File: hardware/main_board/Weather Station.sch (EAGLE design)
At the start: 38 parts, among them J2 RJ12, Q1 200mA/40V, Q2 220mA/50V/3.5Ω, U1 328P, U2 MCP1703T-3302E/CB, U3 W25X40CLSNIG, U4 TL431BQPK, X2 B2B-PH-K-S, X3 B2B-XH-2, Y1 8MHz

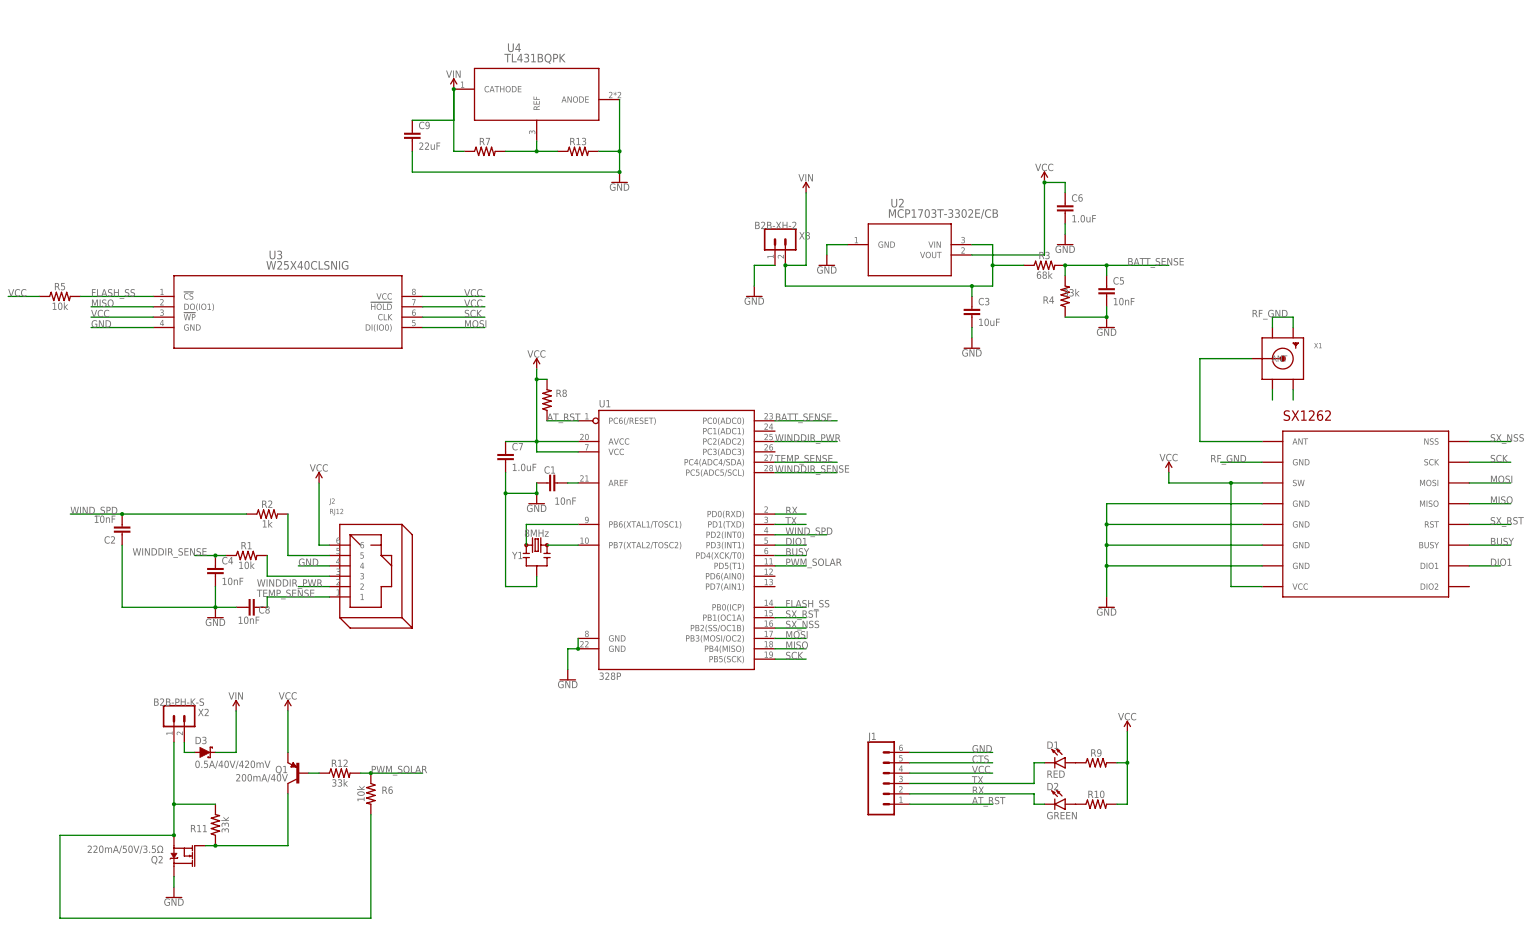
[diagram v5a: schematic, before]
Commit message: Better speed formatting for null values; Some other stuff
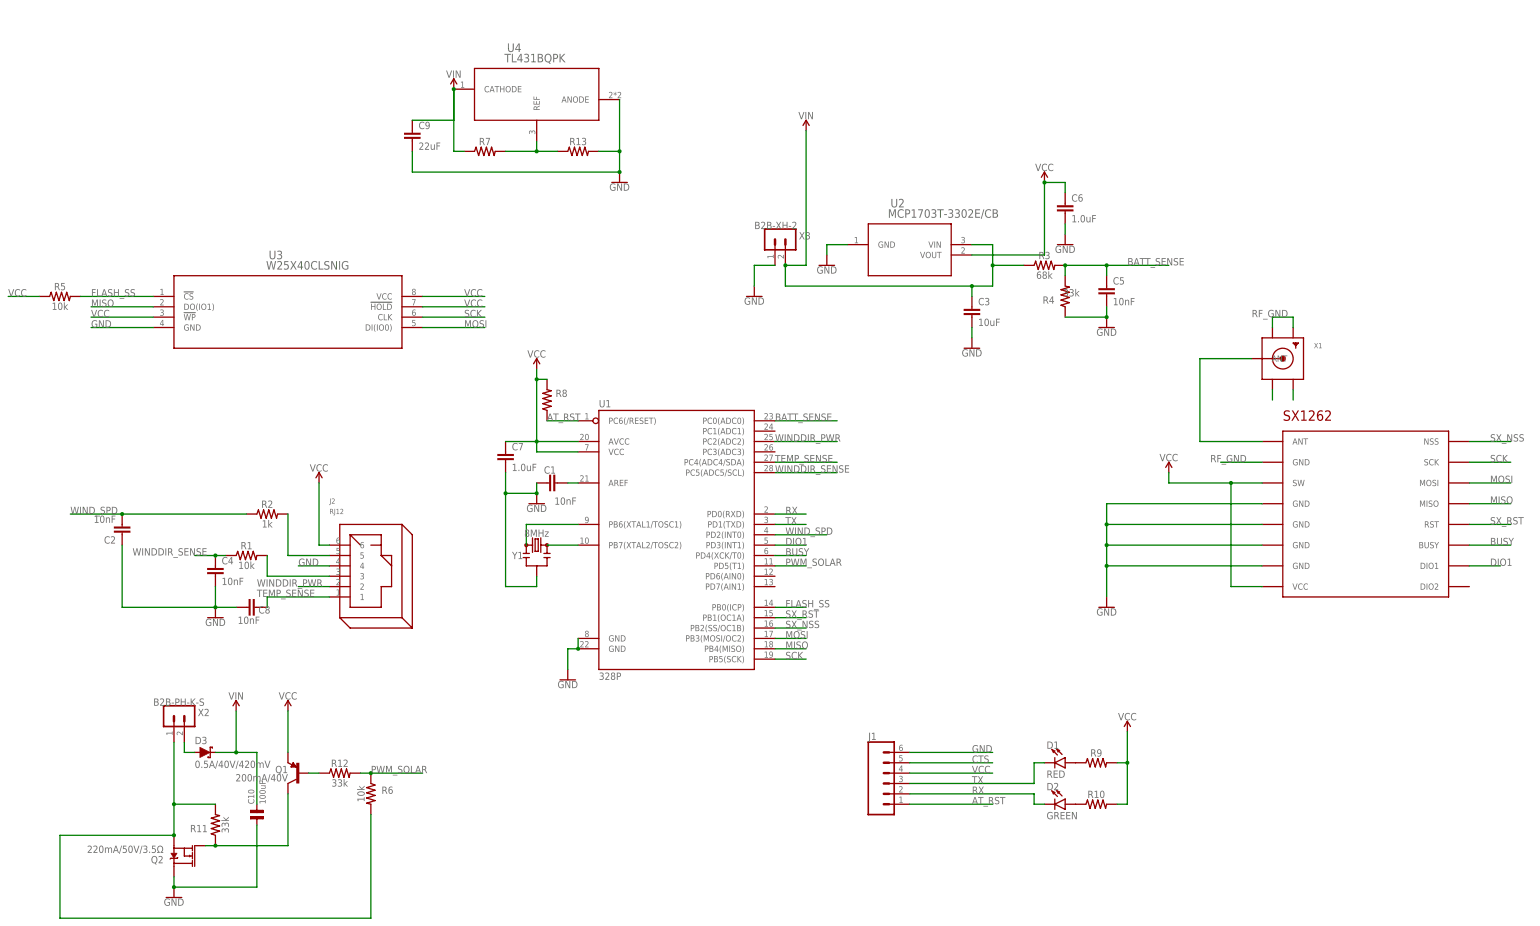
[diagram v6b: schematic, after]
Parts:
- added C10: 100uF, capsmd:C1206
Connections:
- net GND: now also C10.1
- net VIN: now also C10.2
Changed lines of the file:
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@@
 <part name="SUPPLY9" library="SparkFun-PowerSymbols" library_urn="urn:adsk.eagle:library:530" deviceset="VCC" device=""/>
 <part name="U$1" library="RadioShield" deviceset="SX1262" device=""/>
+<part name="C10" library="capsmd" deviceset="C1206" device="" value="100uF"/>
 </parts>
 <sheets>
@@
 <attribute name="VALUE" x="-45.72" y="-21.844" size="1.778" layer="96" font="vector" align="top-center"/>
 </instance>
-<instance part="SUPPLY5" gate="G$1" x="68.58" y="121.92" smashed="yes">
-<attribute name="VALUE" x="68.58" y="124.714" size="1.778" layer="96" align="bottom-center"/>
+<instance part="SUPPLY5" gate="G$1" x="68.58" y="137.16" smashed="yes">
+<attribute name="VALUE" x="68.58" y="139.954" size="1.778" layer="96" align="bottom-center"/>
 </instance>
 <instance part="SUPPLY7" gate="G$1" x="-71.12" y="-5.08" smashed="yes">
@@
 </instance>
 <instance part="U$1" gate="G$1" x="205.74" y="43.18" smashed="yes"/>
+<instance part="C10" gate="G$1" x="-66.04" y="-30.48" smashed="yes" rot="R90">
+<attribute name="NAME" x="-66.675" y="-27.94" size="1.524" layer="95" rot="R90"/>
+<attribute name="VALUE" x="-63.881" y="-27.94" size="1.524" layer="96" rot="R90"/>
+</instance>
 </instances>
 <busses>
@@
 </segment>
 <segment>
+<pinref part="GND8" gate="1" pin="GND"/>
 <pinref part="C3" gate="G$1" pin="2"/>
-<pinref part="GND8" gate="1" pin="GND"/>
 <wire x1="109.22" y1="88.9" x2="109.22" y2="86.36" width="0.1524" layer="91"/>
+</segment>
+<segment>
+<pinref part="C10" gate="G$1" pin="1"/>
+<pinref part="Q2" gate="NMOS" pin="D"/>
+<pinref part="GND10" gate="1" pin="GND"/>
+<wire x1="-86.36" y1="-45.72" x2="-86.36" y2="-48.26" width="0.1524" layer="91"/>
+<wire x1="-66.04" y1="-33.02" x2="-66.04" y2="-48.26" width="0.1524" layer="91"/>
+<wire x1="-66.04" y1="-48.26" x2="-86.36" y2="-48.26" width="0.1524" layer="91"/>
+<junction x="-86.36" y="-48.26"/>
 </segment>
 <segment>
@@
 <wire x1="-91.44" y1="88.9" x2="-106.68" y2="88.9" width="0.1524" layer="91"/>
 <label x="-106.68" y="88.9" size="1.778" layer="95"/>
-</segment>
-<segment>
-<pinref part="Q2" gate="NMOS" pin="D"/>
-<pinref part="GND10" gate="1" pin="GND"/>
-<wire x1="-86.36" y1="-45.72" x2="-86.36" y2="-48.26" width="0.1524" layer="91"/>
 </segment>
 <segment>
@@
 <net name="VIN" class="0">
 <segment>
+<pinref part="SUPPLY7" gate="G$1" pin="VIN"/>
+<pinref part="C10" gate="G$1" pin="2"/>
+<wire x1="-66.04" y1="-15.24" x2="-66.04" y2="-27.94" width="0.1524" layer="91"/>
+<pinref part="D3" gate="G$1" pin="C"/>
+<wire x1="-76.2" y1="-15.24" x2="-71.12" y2="-15.24" width="0.1524" layer="91"/>
+<wire x1="-71.12" y1="-15.24" x2="-66.04" y2="-15.24" width="0.1524" layer="91"/>
+<junction x="-71.12" y="-15.24"/>
+<wire x1="-71.12" y1="-15.24" x2="-71.12" y2="-5.08" width="0.1524" layer="91"/>
+</segment>
+<segment>
 <wire x1="63.5" y1="104.14" x2="63.5" y2="99.06" width="0.1524" layer="91"/>
 <wire x1="63.5" y1="99.06" x2="109.22" y2="99.06" width="0.1524" layer="91"/>
@@
 <wire x1="114.3" y1="109.22" x2="114.3" y2="104.14" width="0.1524" layer="91"/>
 <wire x1="63.5" y1="104.14" x2="68.58" y2="104.14" width="0.1524" layer="91"/>
-<wire x1="68.58" y1="104.14" x2="68.58" y2="121.92" width="0.1524" layer="91"/>
+<wire x1="68.58" y1="104.14" x2="68.58" y2="137.16" width="0.1524" layer="91"/>
 <junction x="63.5" y="104.14"/>
 <pinref part="SUPPLY5" gate="G$1" pin="VIN"/>
 </segment>
 <segment>
-<pinref part="D3" gate="G$1" pin="C"/>
-<pinref part="SUPPLY7" gate="G$1" pin="VIN"/>
-<wire x1="-76.2" y1="-15.24" x2="-71.12" y2="-15.24" width="0.1524" layer="91"/>
-<wire x1="-71.12" y1="-15.24" x2="-71.12" y2="-5.08" width="0.1524" layer="91"/>
-</segment>
-<segment>

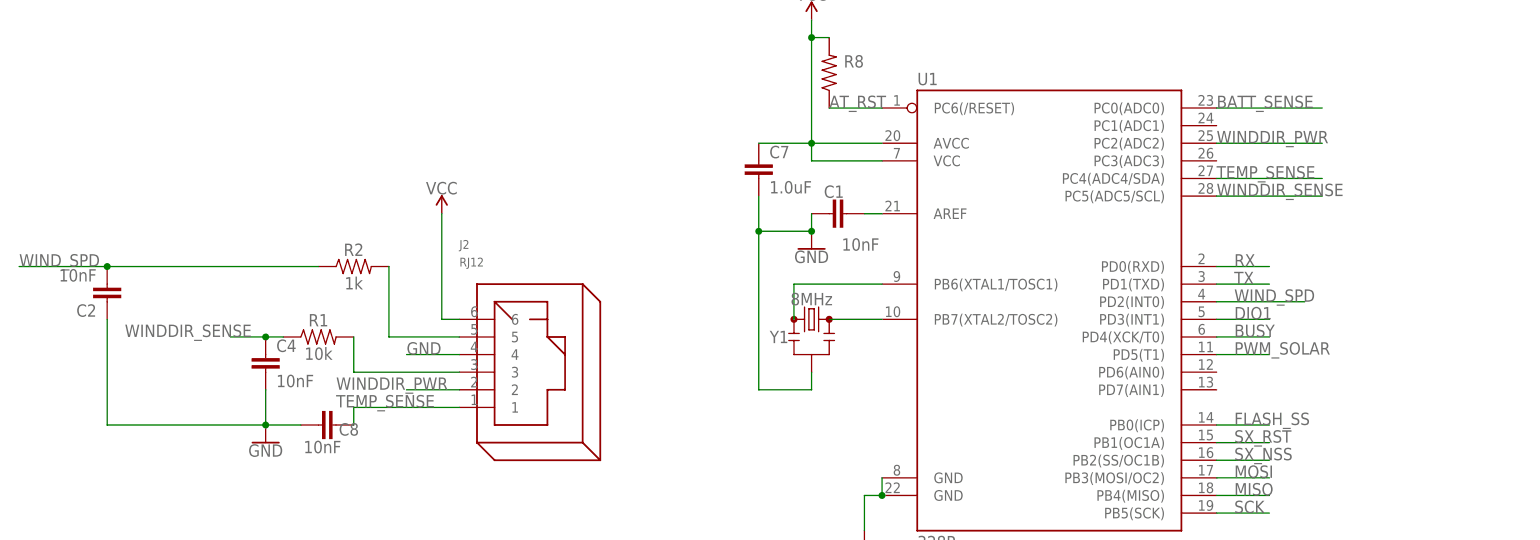
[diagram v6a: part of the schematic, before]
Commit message: ALS Wind direction bug fixes. Added ability to chain receivers using UDP. QueryVolatileResponse bugfix.
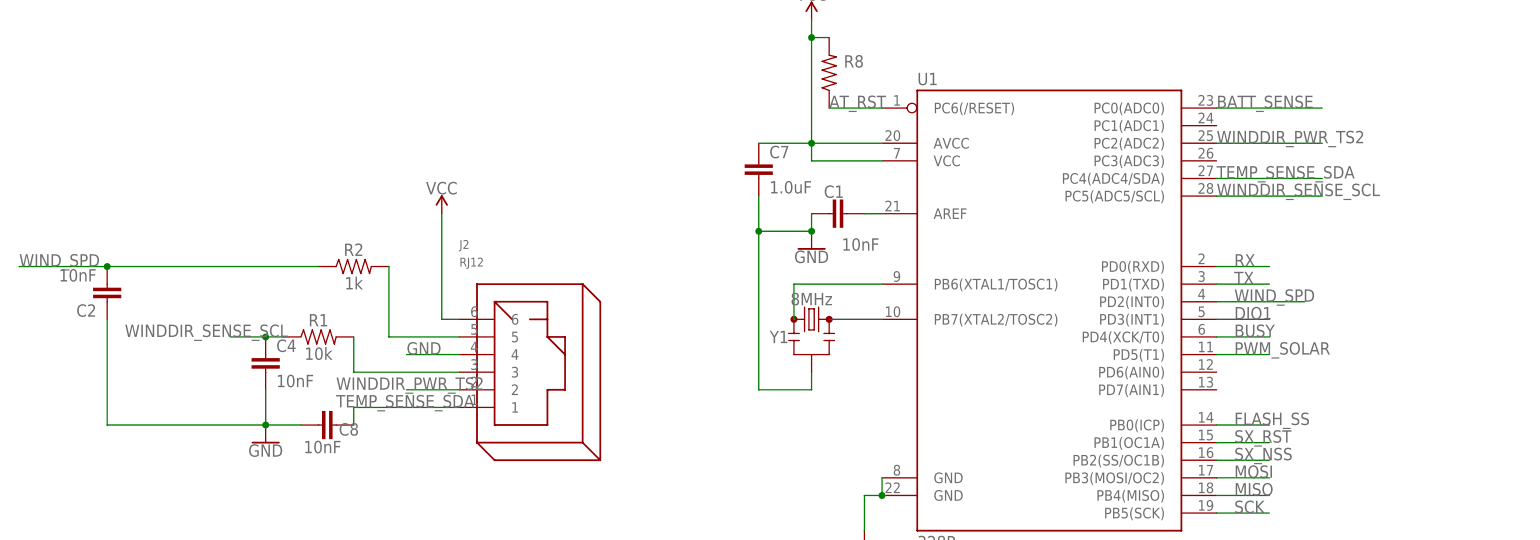
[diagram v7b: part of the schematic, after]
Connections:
- net TEMP_SENSE renamed TEMP_SENSE_SDA
- net WINDDIR_PWR renamed WINDDIR_PWR_TS2
- net WINDDIR_SENSE renamed WINDDIR_SENSE_SCL
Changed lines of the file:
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@@
 </segment>
 </net>
-<net name="WINDDIR_PWR" class="0">
+<net name="WINDDIR_PWR_TS2" class="0">
 <segment>
 <pinref part="U1" gate="G$1" pin="PC2(ADC2)"/>
@@
 </segment>
 </net>
-<net name="WINDDIR_SENSE" class="0">
+<net name="WINDDIR_SENSE_SCL" class="0">
 <segment>
 <pinref part="C4" gate="G$1" pin="1"/>
@@
 </segment>
 </net>
-<net name="TEMP_SENSE" class="0">
+<net name="TEMP_SENSE_SDA" class="0">
 <segment>
 <pinref part="J2" gate="G$1" pin="1"/>
